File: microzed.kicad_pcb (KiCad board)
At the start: 10 copper layers, 60 x 100 mm, 333 parts, among them IC1 XC7Z020-1CLG484C, IC2 RTL8211E-VL-CG, J1 640456-3, J2 10104111-0001LF, J3 L829-1J1T-43, J4 Micro_SD_Card_Det_Hirose_DM3AT, J5 10104111-0001LF, J6 BSH-090-01-X-D-A, J7 BSH-090-01-X-D-A, Q1 MMBT3904, Q2 MMBT3904, SW1 SW_Push, U1 TLV62130RGTR, U10 MT41K256M16TW, U11 MT25QL128ABA8E12-1SIT, U12 USB3320C-EZK, U13 ASDMB-24.000MHZ-LC-T, U14 ASDMB-25.000MHZ-LC-T, U15 TXS02612RTWR, U16 CP2104-F03-GM, U2 TLV62130RGTR, U3 TLV62130RGTR, U4 TLV62130RGTR, U5 TLV62130RGTR, U6 ASDMB-33.333MHZ-LC-T, U7 TPS51206DSQR, U8 REF3012, U9 MT41K256M16TW

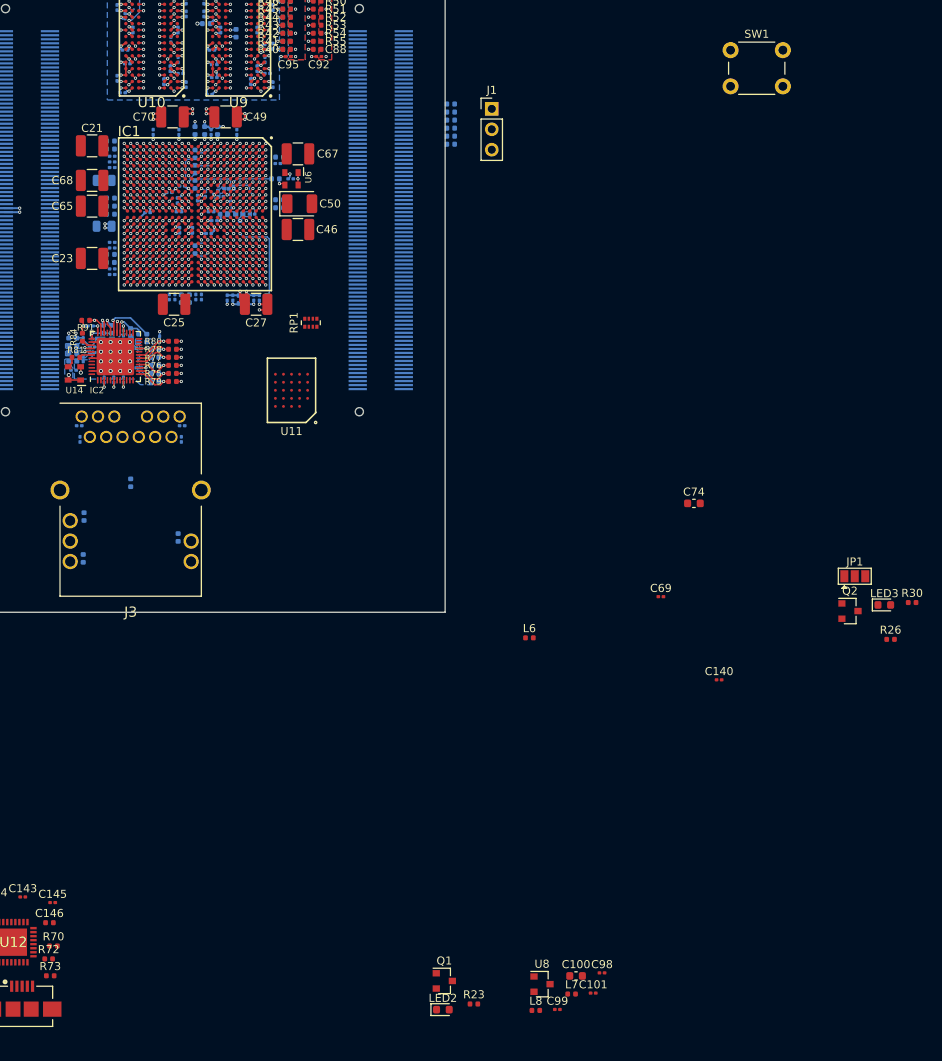
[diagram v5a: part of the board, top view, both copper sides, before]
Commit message: qspi reset: add level translator
Signed-off-by: Yi Qingliang <niqingliang2003@gmail.com>
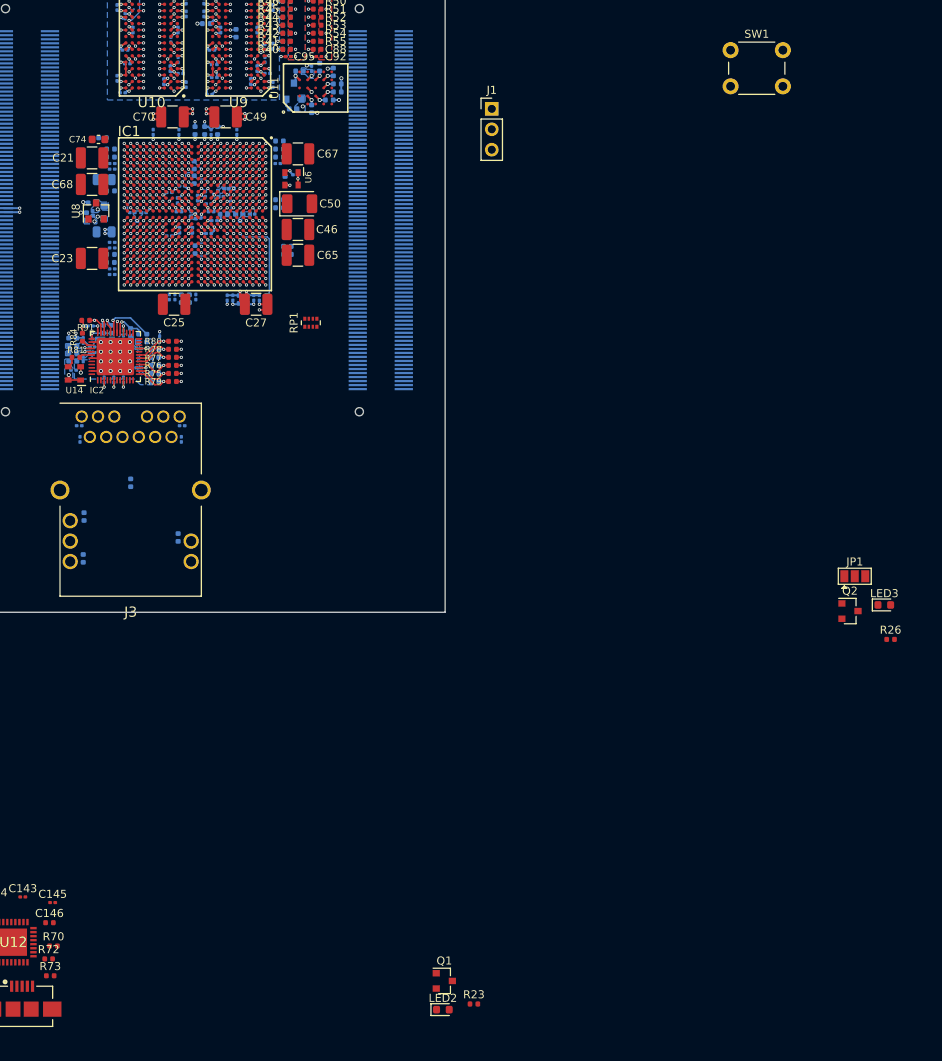
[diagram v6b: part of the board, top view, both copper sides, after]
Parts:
- added Q3: BSS138, Package_TO_SOT_SMD:SOT-23, B.Cu at (11.2, 35.2)
- added R105: 10K, Resistor_SMD:R_0402_1005Metric, B.Cu at (15.6, 36.3)
- added R106: 10K, Resistor_SMD:R_0402_1005Metric, B.Cu at (11.9, 32.7)
- C100, C101, C140, C69, C98, C99, L6, L7, L8, R30: moved to B.Cu
- moved L7 115.0 mm to (-13.9, 49.1)
- moved C99 114.6 mm to (-13.8, 50.4), turned to 90 degrees
- moved L8 113.4 mm to (-14.6, 50.8), turned to 270 degrees
- moved C100 111.6 mm to (-12.4, 50.3), turned to 90 degrees
- moved U8 111.0 mm to (-13.4, 50.1), turned to 90 degrees
- moved C101 109.0 mm to (-1.60, 50.5), turned to 270 degrees
- moved C98 106.4 mm to (-0.70, 51.0), turned to 180 degrees
- moved R30 97.6 mm to (16.1, 32.8), turned to 270 degrees
- moved C140 91.3 mm to (13.4, 32.4), turned to 90 degrees
- moved C74 86.8 mm to (-13.1, 41.2), turned to 180 degrees
- moved L6 81.8 mm to (-12.6, 41.0)
- moved C69 73.6 mm to (0.90, 50.2), turned to 180 degrees
- moved U11 37.7 mm to (13.9, 34.8), turned to 90 degrees
- moved C65 26.3 mm to (11.7, 55.6), turned to 0 degrees
- moved C53 22.6 mm to (10.4, 55.5), turned to 0 degrees
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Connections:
- U11 pad A4: CARRIER_SRST# -> Net-(Q3-Pad3)
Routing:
- net CARRIER_SRST#: track 9.17 -> 1.92 mm
- net Net-(IC1-PadF7): track 5.43 -> 0.57 mm
- net GND: track 145.0 -> 148.5 mm, vias 198 -> 203
- net V3V3: track 29.8 -> 32.4 mm, vias 23 -> 26
- net Net-(Q3-Pad3): track 0.00 -> 2.30 mm, vias 0 -> 1
- net VCCO_13: track 4.57 -> 6.44 mm
- net Net-(IC1-PadN7): track 4.69 -> 3.06 mm
- net VREFP: track 0.57 -> 2.09 mm, vias 1 -> 2
- net QSPI_CS#: track 0.57 -> 1.99 mm, vias 1 -> 2
- net QSPI_DQ1: track 0.57 -> 1.99 mm, vias 1 -> 2
- net QSPI_DQ0: track 0.57 -> 1.99 mm, vias 1 -> 2
- net QSPI_DQ3: track 0.57 -> 1.97 mm, vias 1 -> 2
- net QSPI_SCK: track 0.57 -> 1.89 mm, vias 1 -> 2
- net QSPI_DQ2: track 0.57 -> 1.89 mm, vias 1 -> 2
- net Net-(IC1-PadM7): track 2.07 -> 1.34 mm
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- added copper zone on B.Cu, net GNDADC
- added copper zone on B.Cu, net VCCADC

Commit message: elements located nearly done
Signed-off-by: Yi Qingliang <niqingliang2003@gmail.com>
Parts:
- C141, C142, C143, C144, C145, C171, C172, C174, C175, C176, C181, C5, C6, C9, D1, D2, J4, L3, R100, R102, R12, R13, R26, R6, R7, R70, R96, R97, R98, R99, U3: moved to B.Cu
- D3: footprint Diode_SMD:D_SMC -> Diode_SMD:D_SMA
- moved D3 143.3 mm to (-23.5, 19.0)
- moved LED2 127.5 mm to (40.7, 22.4)
- moved Q1 127.5 mm to (40.9, 18.8)
- moved R23 127.5 mm to (44.6, 21.7)
- moved C172 107.8 mm to (-24.1, 78.7), turned to 90 degrees
- moved R100 105.8 mm to (-24.7, 74.0)
- moved R101 103.6 mm to (-26.9, 78.9), turned to 270 degrees
- moved D2 102.2 mm to (-25.8, 82.2)
- moved U16 102.0 mm to (-23.9, 76.9)
- moved R102 101.8 mm to (-24.7, 75.0)
- moved C181 99.7 mm to (13.7, 83.0), turned to 270 degrees
- moved C5 97.4 mm to (14.1, 85.6), turned to 270 degrees
- moved C174 96.6 mm to (-26.9, 76.7), turned to 90 degrees
- moved R103 96.0 mm to (-24.9, 80.0), turned to 180 degrees
- moved C6 95.9 mm to (13.1, 81.4)
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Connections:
- Q3 pad 2: CARRIER_SRST# -> Net-(Q3-Pad2)
- Q3 pad 3: Net-(Q3-Pad3) -> CARRIER_SRST#
- R106 pad 2: Net-(Q3-Pad3) -> CARRIER_SRST#
- U11 pad A4: Net-(Q3-Pad3) -> CARRIER_SRST#
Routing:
- net PWR_B501: track 22.9 -> 29.4 mm, vias 21 -> 25
- net V3V3: track 32.4 -> 34.8 mm, vias 26 -> 27
- net Net-(Q3-Pad3): track 2.30 -> 0.00 mm, vias 1 -> 0
- net CARRIER_SRST#: track 1.92 -> 4.21 mm, vias 1 -> 2
- net BANK13_LVDS_6_N: track 2.53 -> 0.57 mm, vias 2 -> 1
- net Net-(R70-Pad1): track 0.00 -> 1.47 mm, vias 0 -> 1
- net Net-(R71-Pad1): track 0.00 -> 1.08 mm
- net Net-(R71-Pad2): track 0.00 -> 0.98 mm
- net GND: track 148.5 -> 148.0 mm, vias 203 -> 211
- net Net-(C175-Pad1): vias 0 -> 1
- net (no net): vias 0 -> 6
- added copper zone on In8.Cu.VCC, net GND
- removed copper zone on In8.Cu.VCC, net VIN
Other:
- board size 60 x 100 mm -> 60 x 90 mm

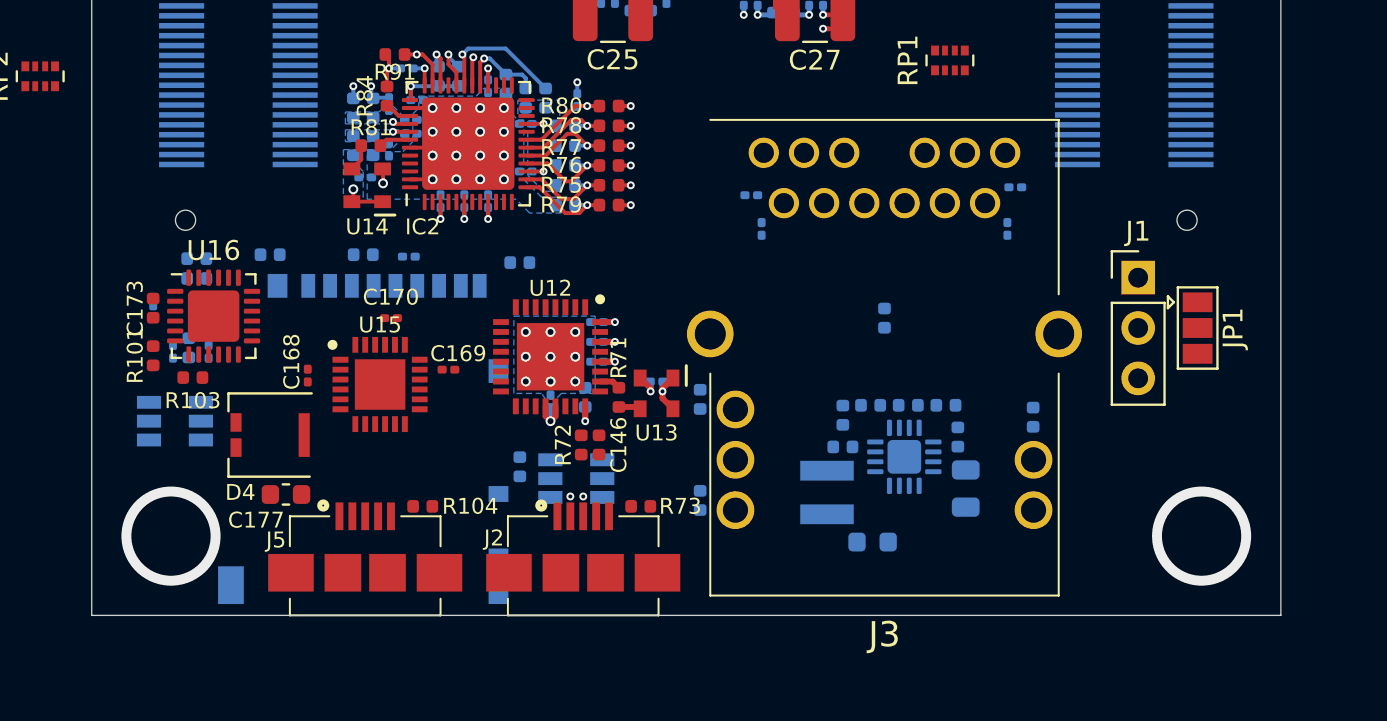
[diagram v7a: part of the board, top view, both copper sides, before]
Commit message: check rj45 connector, try to find smaller footprint
Signed-off-by: Yi Qingliang <niqingliang2003@gmail.com>
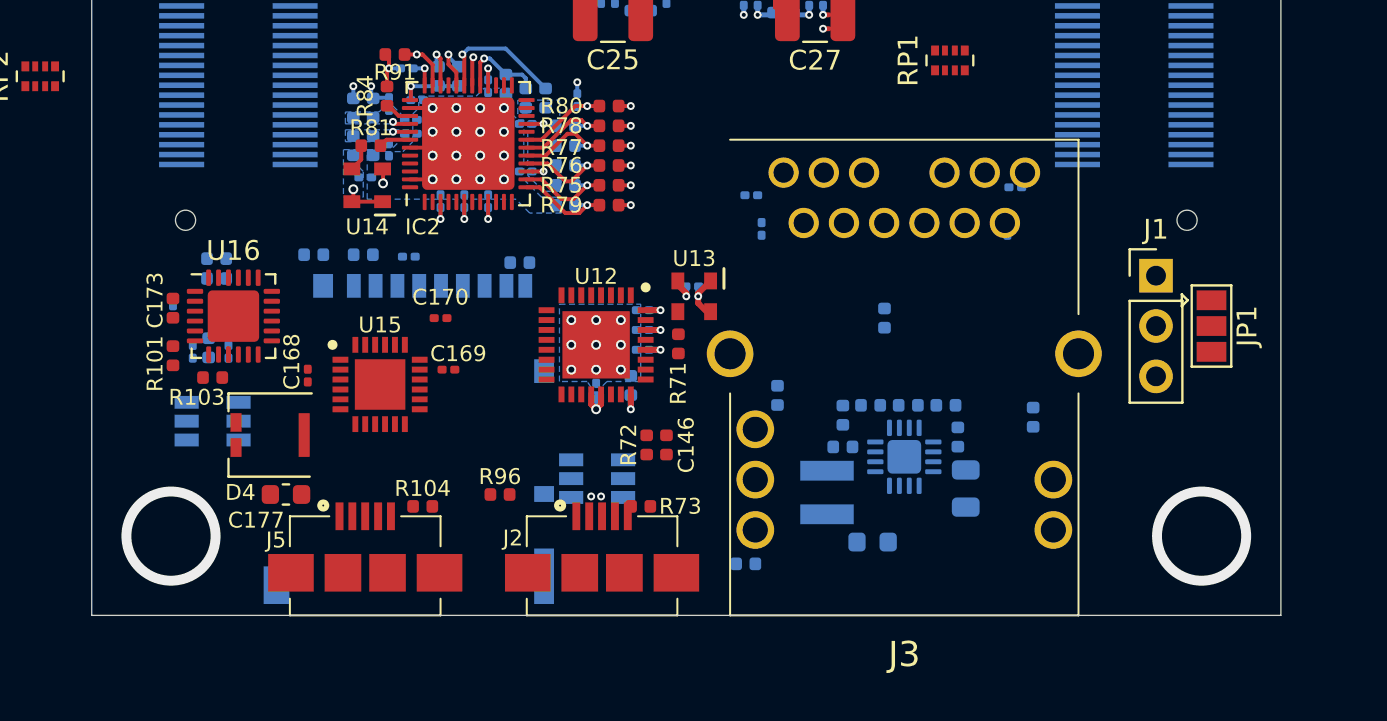
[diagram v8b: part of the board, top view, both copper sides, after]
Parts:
- R96: moved to F.Cu
- moved U13 5.26 mm to (0.40, 75.9)
- moved C141 5.13 mm to (0.30, 75.4)
- moved R71 4.04 mm to (-0.40, 78.3)
- moved R88 3.94 mm to (3.00, 89.4), turned to 180 degrees
- moved R89 3.91 mm to (4.60, 80.9)
- moved C146 3.40 mm to (-1.00, 83.4)
- moved R72 3.30 mm to (-2.00, 83.4)
- moved C170 2.50 mm to (-12.4, 77.0)
- moved C142 2.38 mm to (-4.55, 80.6)
- moved C143 2.38 mm to (-2.20, 78.6)
- moved C144 2.38 mm to (-2.20, 76.6)
- moved C145 2.38 mm to (-2.20, 77.6)
- moved U12 2.38 mm to (-4.55, 78.3)
- moved R70 2.38 mm to (-2.80, 80.4)
- moved J4 2.30 mm to (-14.0, 83.1)
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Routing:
- net Net-(R71-Pad1): track 1.08 -> 0.00 mm
- net Net-(R71-Pad2): track 0.98 -> 0.00 mm
- net GND: vias 211 -> 213
- net (no net): vias 6 -> 4
